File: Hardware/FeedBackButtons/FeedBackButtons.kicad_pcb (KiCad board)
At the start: 2 copper layers, 37.2 x 35.6 mm, 15 parts, among them J1 Barrel_Jack_MountingPin, J2 RJ45, U1 ESP8266-01/ESP-01, U2 AMS1117-3.3, U3 4N25

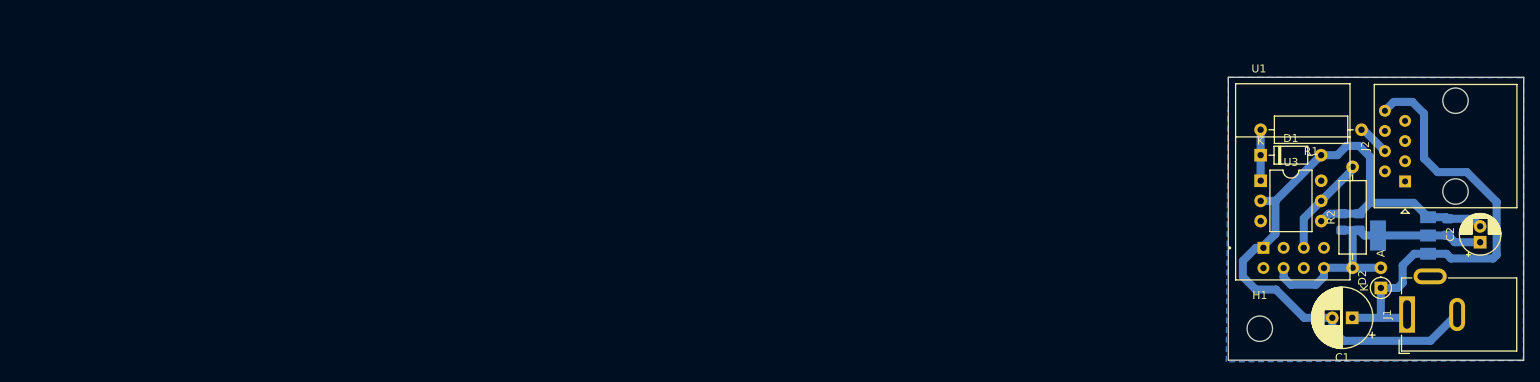
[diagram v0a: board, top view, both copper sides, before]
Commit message: Diseño esquematico y pcb con ruteado
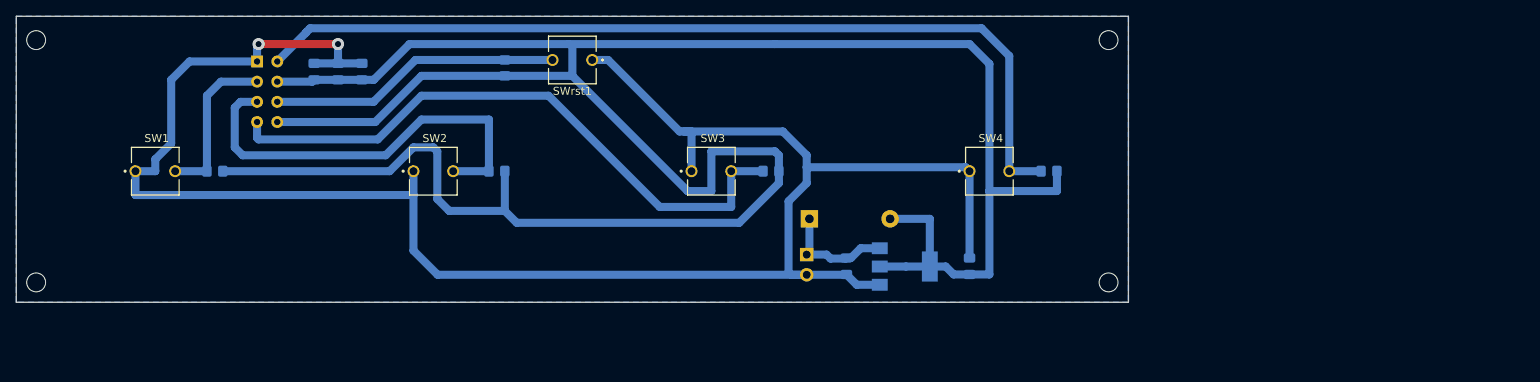
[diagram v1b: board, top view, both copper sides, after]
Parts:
- removed D1: 1N4148, Diode_THT:D_DO-35_SOD27_P7.62mm_Horizontal
- removed H1: MountingHole, MountingHole:MountingHole_3.2mm_M3
- removed J1: Barrel_Jack_MountingPin, Connector_BarrelJack:BarrelJack_GCT_DCJ200-10-A_Horizontal
- removed J2: RJ45, Connector_RJ:RJ45_Amphenol_54602-x08_Horizontal
- removed U3: 4N25, Package_DIP:DIP-6_W7.62mm
- added BT1: Battery_Cell, Connector_PinHeader_2.54mm:PinHeader_1x02_P2.54mm_Horizontal, B.Cu at (129.5, 129.0)
- added R3: R_Small, Resistor_SMD:R_0805_2012Metric_Pad1.20x1.40mm_HandSolder, B.Cu at (125.0, 118.5)
- added R4: R_Small, Resistor_SMD:R_0805_2012Metric_Pad1.20x1.40mm_HandSolder, B.Cu at (160.0, 118.5)
- added Rrst1: R_Small, Resistor_SMD:R_0805_2012Metric_Pad1.20x1.40mm_HandSolder, B.Cu at (91.5, 105.5)
- added SW1: SW_Push, BUTT-2:SW_BUTT-2, F.Cu at (47.5, 118.5)
- added SW2: SW_Push, BUTT-2:SW_BUTT-2, F.Cu at (82.5, 118.5)
- added SW3: SW_Push, BUTT-2:SW_BUTT-2, F.Cu at (117.5, 118.5)
- added SW4: SW_Push, BUTT-2:SW_BUTT-2, F.Cu at (152.5, 118.5)
- added SWrst1: SW_Push, BUTT-2:SW_BUTT-2, F.Cu at (100.0, 104.5)
- C1: footprint Capacitor_THT:CP_Radial_D7.5mm_P2.50mm -> Capacitor_SMD:C_0805_2012Metric_Pad1.18x1.45mm_HandSolder; moved to B.Cu
- C2: footprint Capacitor_THT:CP_Radial_D5.0mm_P2.00mm -> Capacitor_SMD:C_0805_2012Metric_Pad1.18x1.45mm_HandSolder; moved to B.Cu
- D2: footprint Diode_THT:D_DO-35_SOD27_P2.54mm_Vertical_AnodeUp -> Diode_THT:D_DO-41_SOD81_P10.16mm_Horizontal; moved to B.Cu
- R1: value 1K -> R_Small; footprint Resistor_THT:R_Axial_DIN0309_L9.0mm_D3.2mm_P12.70mm_Horizontal -> Resistor_SMD:R_0805_2012Metric_Pad1.20x1.40mm_HandSolder; moved to B.Cu
- R2: value 330 -> R_Small; footprint Resistor_THT:R_Axial_DIN0309_L9.0mm_D3.2mm_P12.70mm_Horizontal -> Resistor_SMD:R_0805_2012Metric_Pad1.20x1.40mm_HandSolder; moved to B.Cu
- U1: moved to B.Cu
- moved R1 144.4 mm to (55.0, 118.5)
- moved C4 141.1 mm to (70.5, 106.0)
- moved U1 139.3 mm to (52.0, 108.5), turned to -90 degrees
- moved C3 130.8 mm to (67.5, 106.0)
- moved C5 127.0 mm to (73.5, 106.0)
- moved R2 108.4 mm to (90.5, 118.5), turned to 180 degrees
- moved D2 72.5 mm to (129.8, 124.5), turned to 0 degrees
- moved C2 64.3 mm to (150.0, 130.5)
- moved C1 64.0 mm to (134.5, 130.5), turned to -90 degrees
- moved U2 62.8 mm to (141.8, 130.5), turned to 0 degrees
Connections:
- net /Input renamed BUTTON2
- R1 pad 1: Net-(J2-Pad4) -> +3.3V
- R1 pad 2: Net-(D1-Pad1) -> BUTTON1
- U1 pad 2: unconnected-(U1-Pad2) -> BUTTON1
- U1 pad 4: unconnected-(U1-Pad4) -> BUTTON3
- U1 pad 5: unconnected-(U1-Pad5) -> BUTTON4
- U1 pad 7: unconnected-(U1-Pad7) -> RST
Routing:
- net +3.3V: track 38.2 -> 325.1 mm
- net GND: track 89.5 -> 243.5 mm, vias 0 -> 2
- net BUTTON4: track 0.00 -> 113.9 mm
- net BUTTON3: track 0.00 -> 78.3 mm
- net +5V: track 58.7 -> 14.6 mm
- net BUTTON2: track 12.7 -> 53.4 mm
- net RST: track 0.00 -> 36.8 mm
- net BUTTON1: track 0.00 -> 20.5 mm
- net Net-(D1-Pad1): track 6.42 -> 0.00 mm
- net Net-(J2-Pad4): track 4.06 -> 0.00 mm
- net (no net): vias 0 -> 4
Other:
- board size 37.2 x 35.6 mm -> 140 x 36 mm
